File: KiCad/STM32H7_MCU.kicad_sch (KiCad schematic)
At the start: 53 parts, among them IC2 SN74LVC1G14DBVR, IC3 STM32H7R7L8H6H, IC4 TLV75718PDRVR, Y1 VXM7-9032-25M0000000

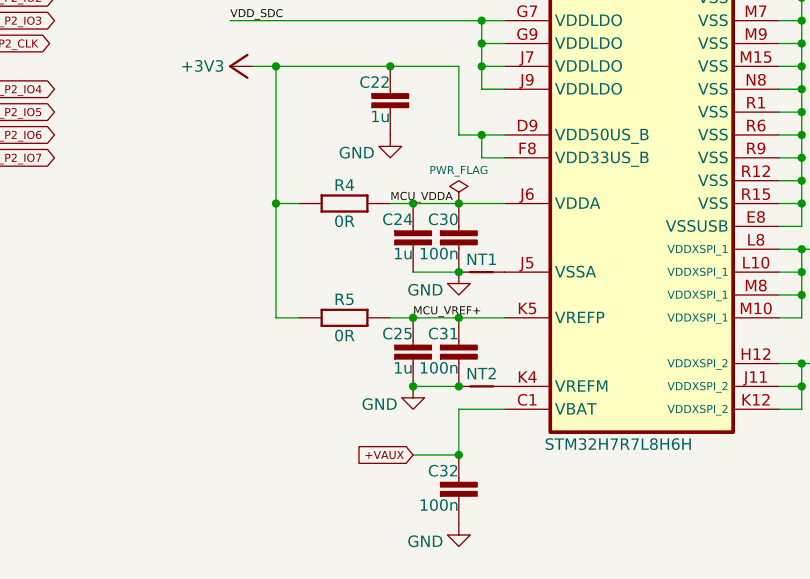
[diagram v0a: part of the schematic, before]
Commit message: BOM update, PCB layout improvements, NetTie positions fixed
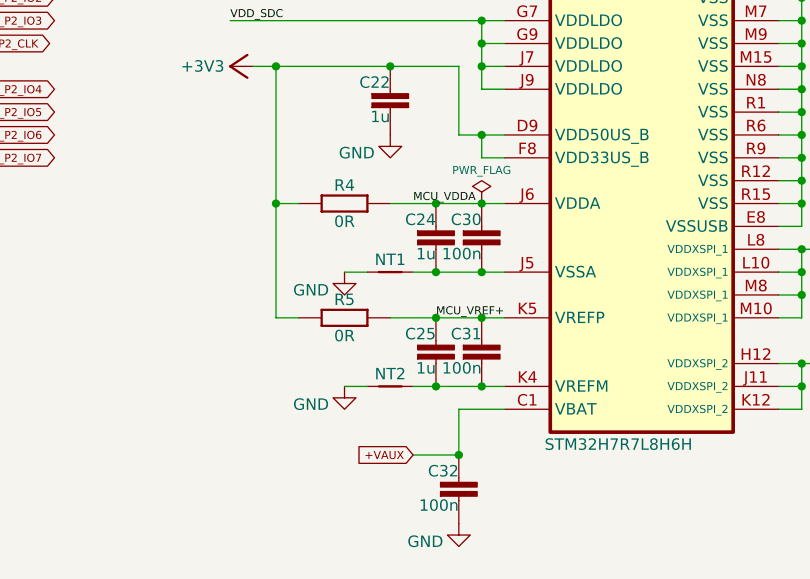
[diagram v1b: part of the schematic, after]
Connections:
- net GND: no longer C24.2, C25.2, C30.2, C31.2
- net at IC3.J5 (VSSA), NT1.2: now also C24.2, C30.2
- net at IC3.K4 (VREFM), NT2.2: now also C25.2, C31.2
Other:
- moved on the sheet: C24, C25, C30, C31, NT1, NT2

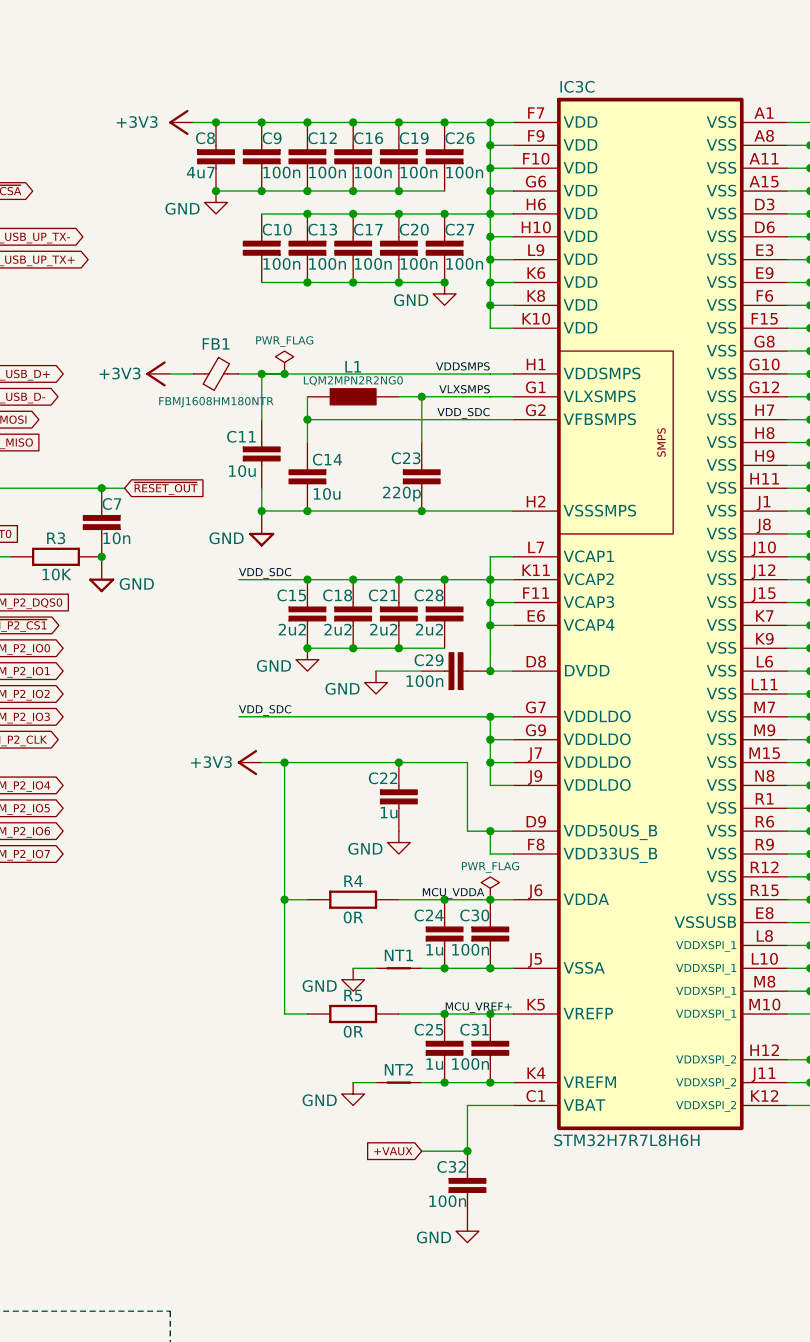
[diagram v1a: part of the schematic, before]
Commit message: Removed all blind/burned vias
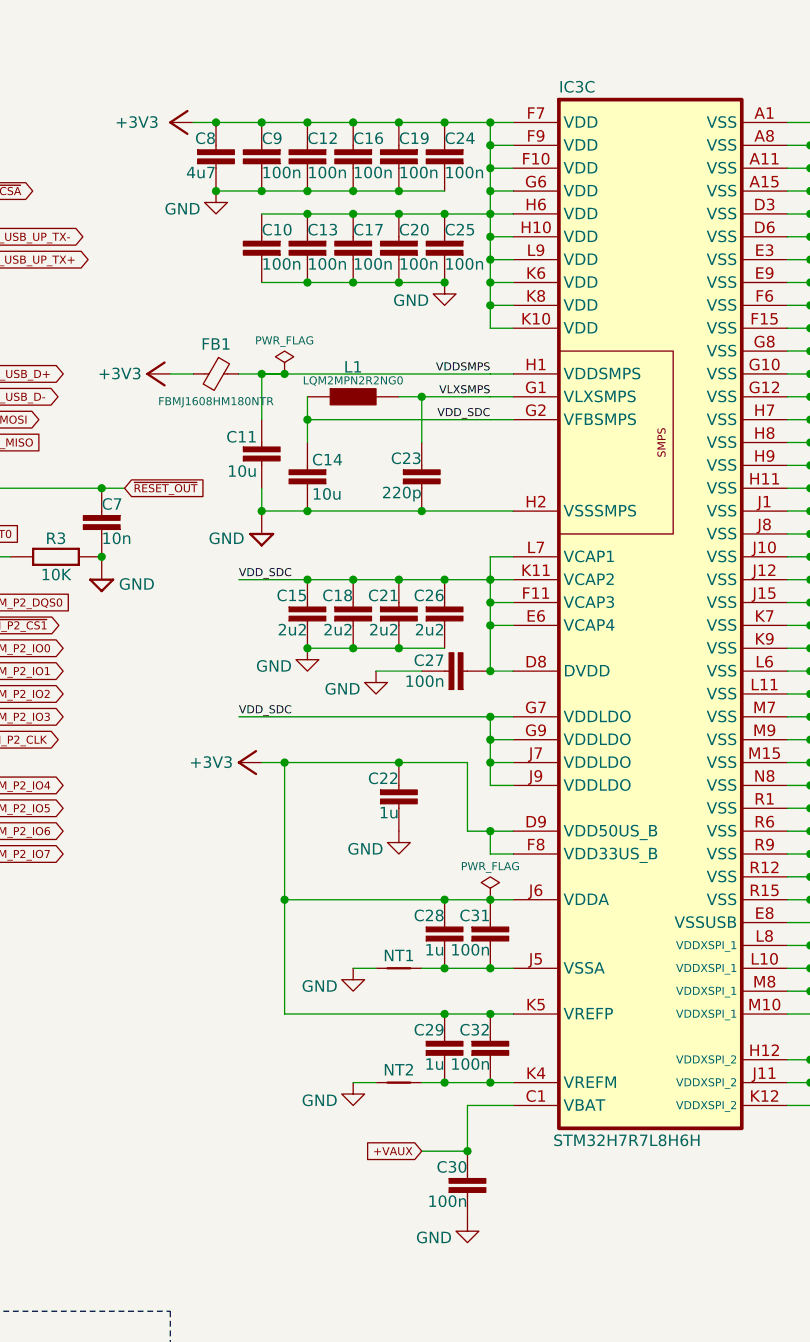
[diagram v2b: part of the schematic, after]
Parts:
- removed R4, R5: 0R, PCM_EEZ_passives:R_0402_1005Metric, symbol PCM_EEZ_passives:R-EU
- C4, C5: footprint PCM_EEZ_passives:C_0603_1608Metric -> PCM_EEZ_passives:C_0402_1005Metric; DigiKey 1276-1069-1-ND -> (none); LCSC C318677 -> (none); Mouser 187-CL10C100CB8NNNC -> (none); TME VJ0603A100JXACW1BC -> (none)
- renumbered C26 to C24, C27 to C25, C28 to C26, C29 to C27, C24 to C28, C25 to C29, C32 to C30, C30 to C31, C31 to C32
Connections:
- net MCU_VDDA is gone; now on net +3V3: C28.1, C31.1, IC3.J6 (VDDA)
- net MCU_VREF+ is gone; now on net +3V3: C29.1, C32.1, IC3.K5 (VREFP)
